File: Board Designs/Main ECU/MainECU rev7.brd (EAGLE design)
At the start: 120.6 x 78.9 mm, 202 parts, among them J1 JUMPER, J2 JUMPER, J3 JUMPER, J4 JUMPER, J5 JUMPER, J6 JUMPER, J7 JUMPER, J8 JUMPER, P1 SOLDER_PAD, P2 SOLDER_PAD, Q1 P-CHANNEL_MOSFET_DMP3099L-7, Q12 P-CHANNEL_MOSFET_DMP3099L-7, X1 CONNECTOR-37, X2 CONNECTOR-4AUTOSPORT, X3 CONNECTOR-4NANO-FIT-VERTICAL-4, X4 CONNECTOR-4NANO-FIT-VERTICAL-4

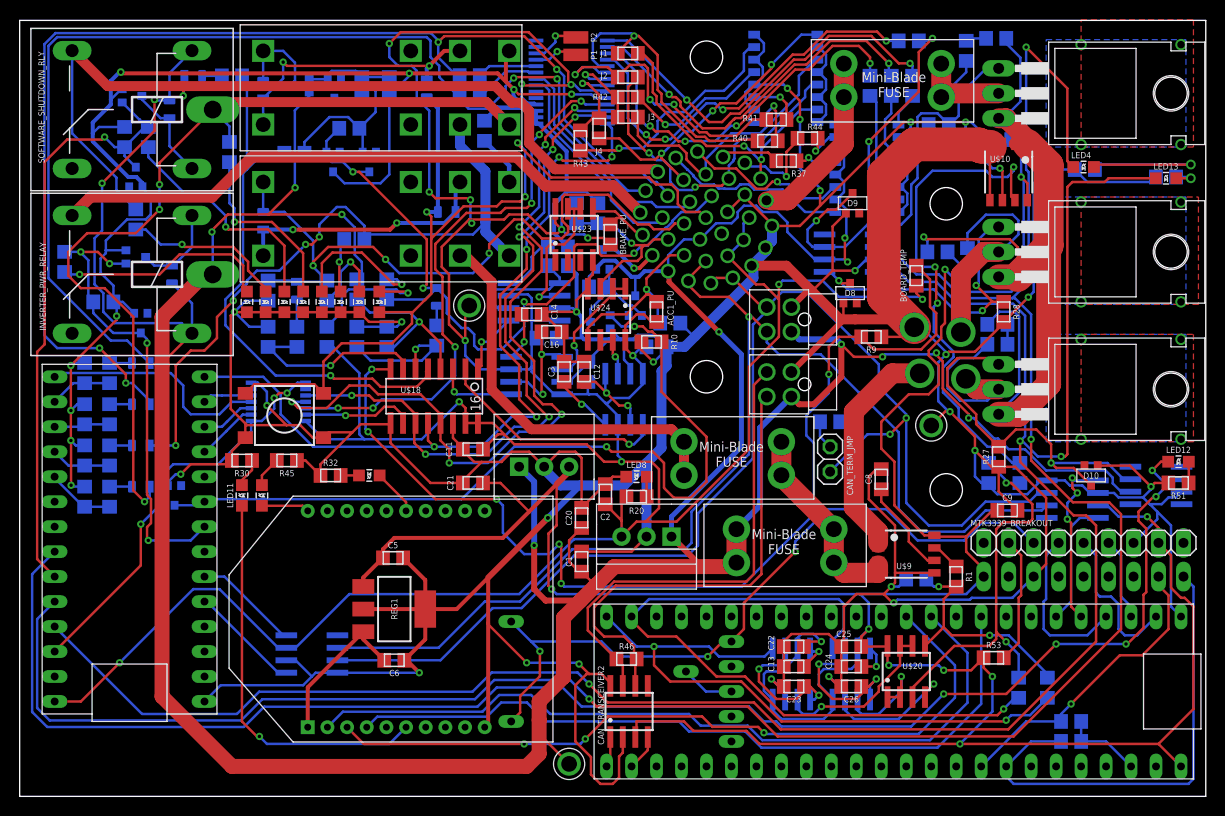
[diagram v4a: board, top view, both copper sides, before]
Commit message: Make silkscreen names larger
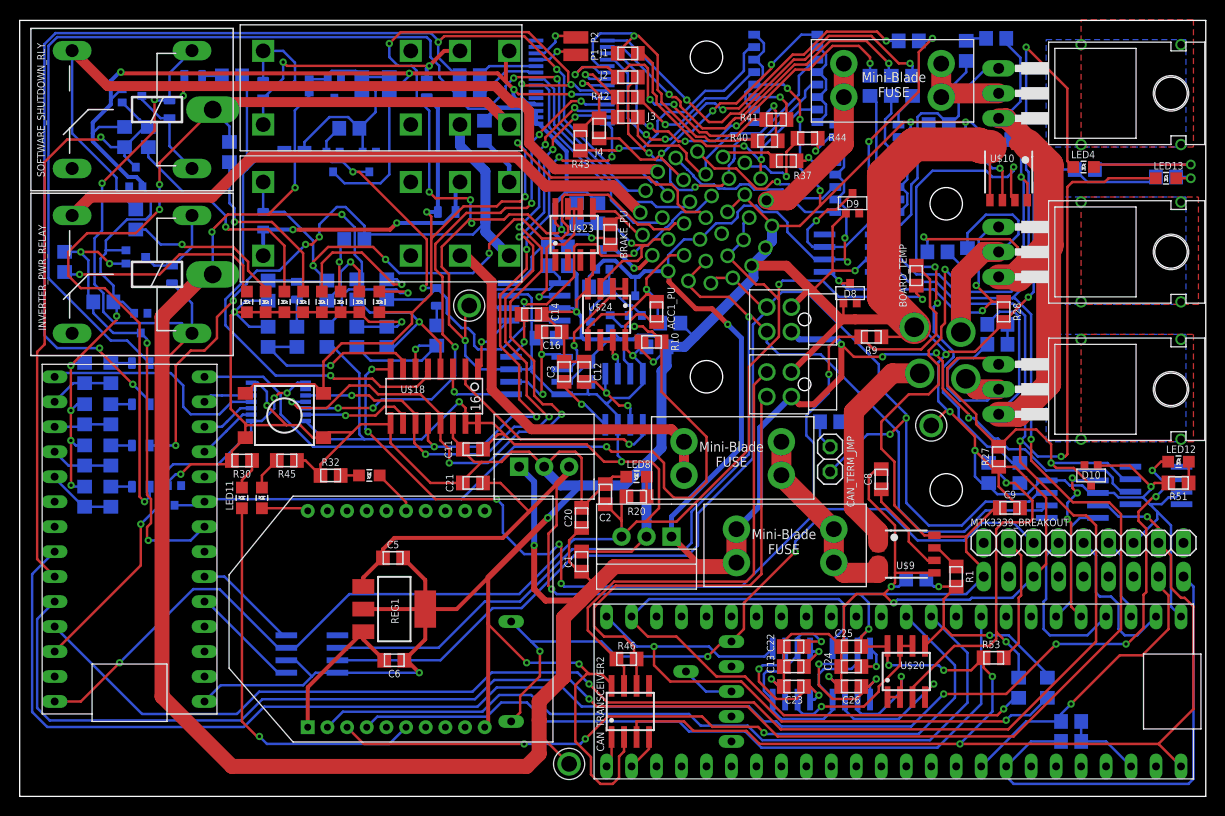
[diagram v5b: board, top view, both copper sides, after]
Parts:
- moved C9 0.36 mm to (100.7, 29.3)
- moved LED11 0.25 mm to (22.6, 30.4)
- moved LED14 0.25 mm to (24.6, 30.4)
- moved CAN_TRANSCEIVER2 0.13 mm to (62.1, 8.64)
- moved R11 0.13 mm to (9.27, 43.1)
- moved R57 0.13 mm to (9.27, 38.9)
- moved R59 0.13 mm to (9.27, 34.7)
- moved R61 0.13 mm to (9.27, 30.5)
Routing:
- net +12V: track 430.3 -> 431.2 mm
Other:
- board text added: "HyTech 2019 Main ECU rev7"
- board text removed: "HyTech 2019 Main ECU rev6"

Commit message: Merged SOT23 package update
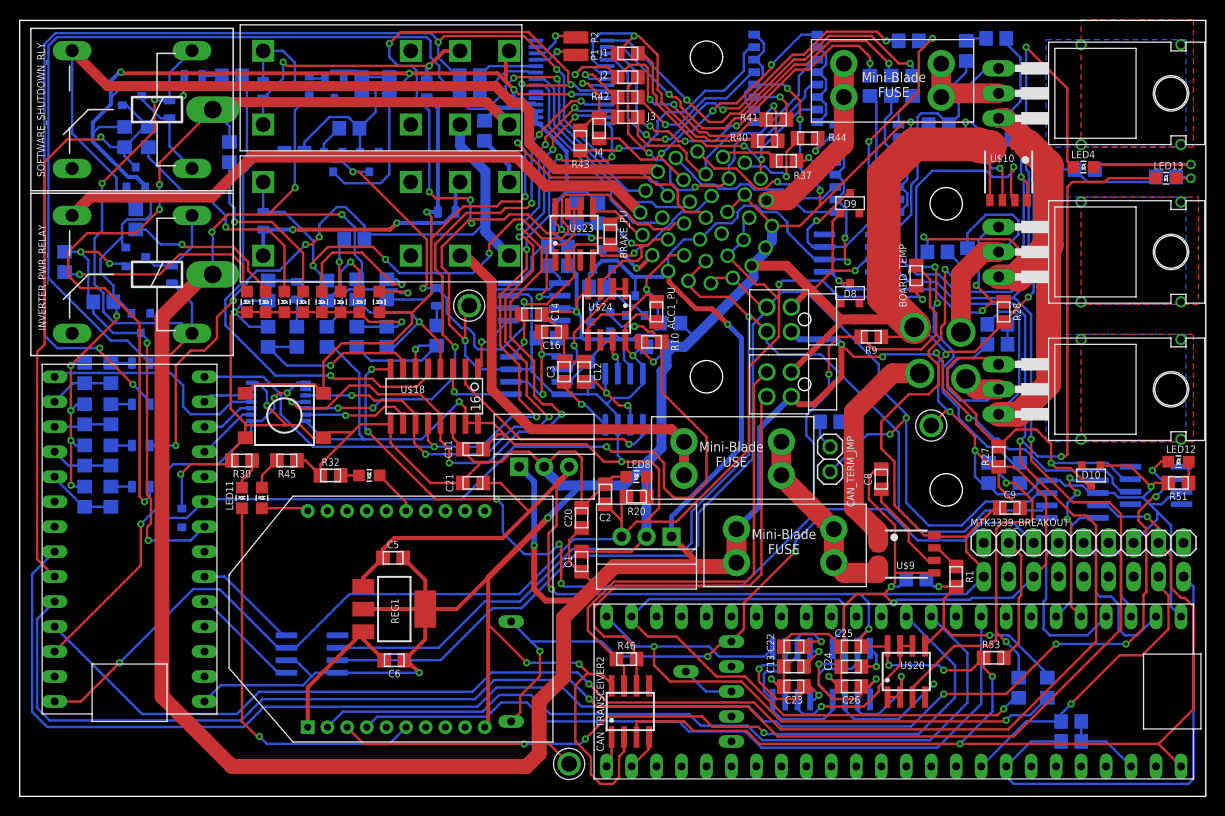
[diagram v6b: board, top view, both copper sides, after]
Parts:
- moved D12 2.30 mm to (15.5, 28.3), turned to 270 degrees
- moved D9 0.25 mm to (84.5, 60.3)
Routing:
- net BRAKE_LIGHT_CTRL: track 83.4 -> 85.5 mm
- net GND: track 918.5 -> 917.5 mm

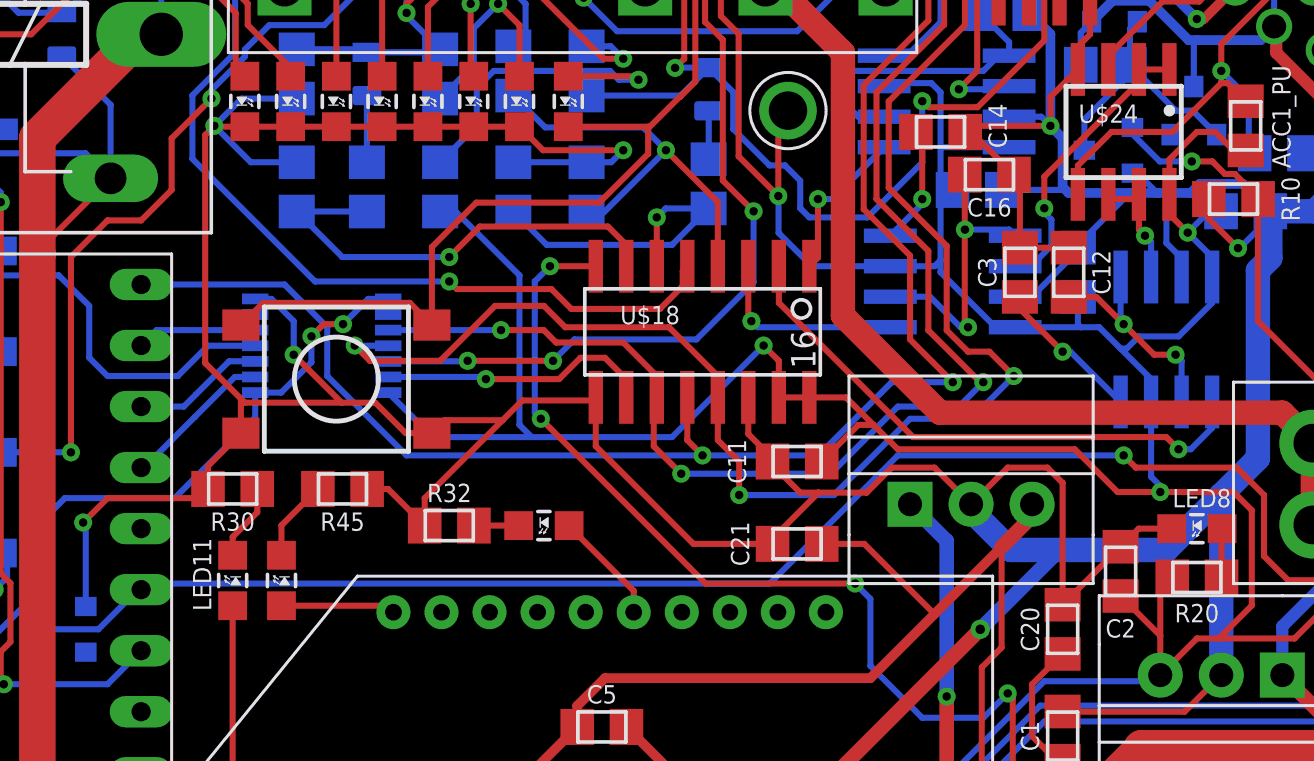
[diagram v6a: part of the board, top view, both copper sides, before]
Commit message: Added second 0.1 capacitor and began moving traces
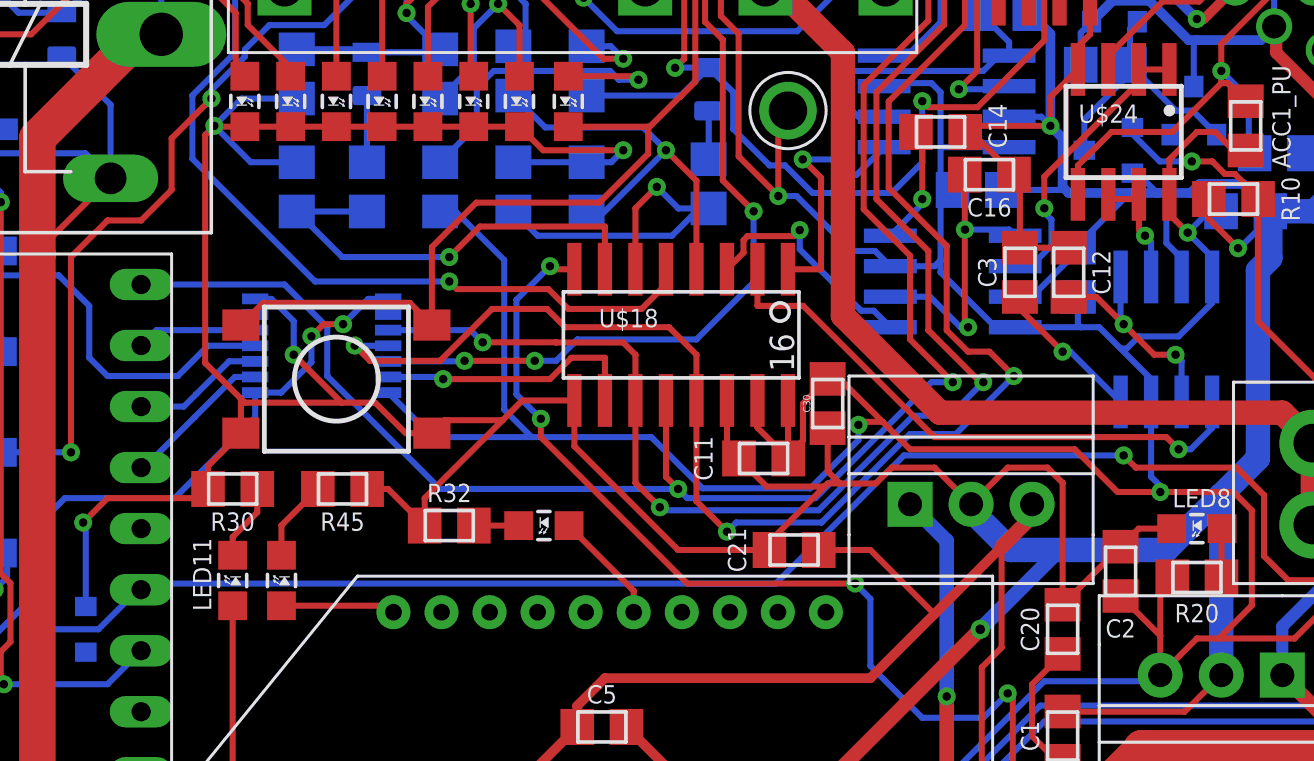
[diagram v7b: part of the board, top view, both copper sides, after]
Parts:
- added C30: 0.1uF, HyTechDevices:0805
- moved C11 1.40 mm to (44.7, 35.4)
- moved U$18 0.90 mm to (41.3, 40.5)
- moved C21 0.28 mm to (46.0, 31.6)
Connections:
- net +5V: now also C30.2
- net GND: now also C30.1
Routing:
- net +5V: track 357.4 -> 364.7 mm
- net READ_BRAKE: track 6.59 -> 10.4 mm
- net GND: track 917.5 -> 921.2 mm
- net MISO_TEENSY: track 81.6 -> 84.3 mm
- net MOSI_5V: track 70.9 -> 73.4 mm
- net SCK_5V: track 79.7 -> 82.1 mm
- net READ_ACCEL2: track 8.23 -> 9.92 mm
- net BMS_OK_READ: track 13.7 -> 15.3 mm
- net BMS_OK: track 74.4 -> 72.9 mm
- net SHUTDOWN_OUT_READ: track 55.3 -> 54.3 mm
- net READ_ACCEL1: track 23.5 -> 24.4 mm

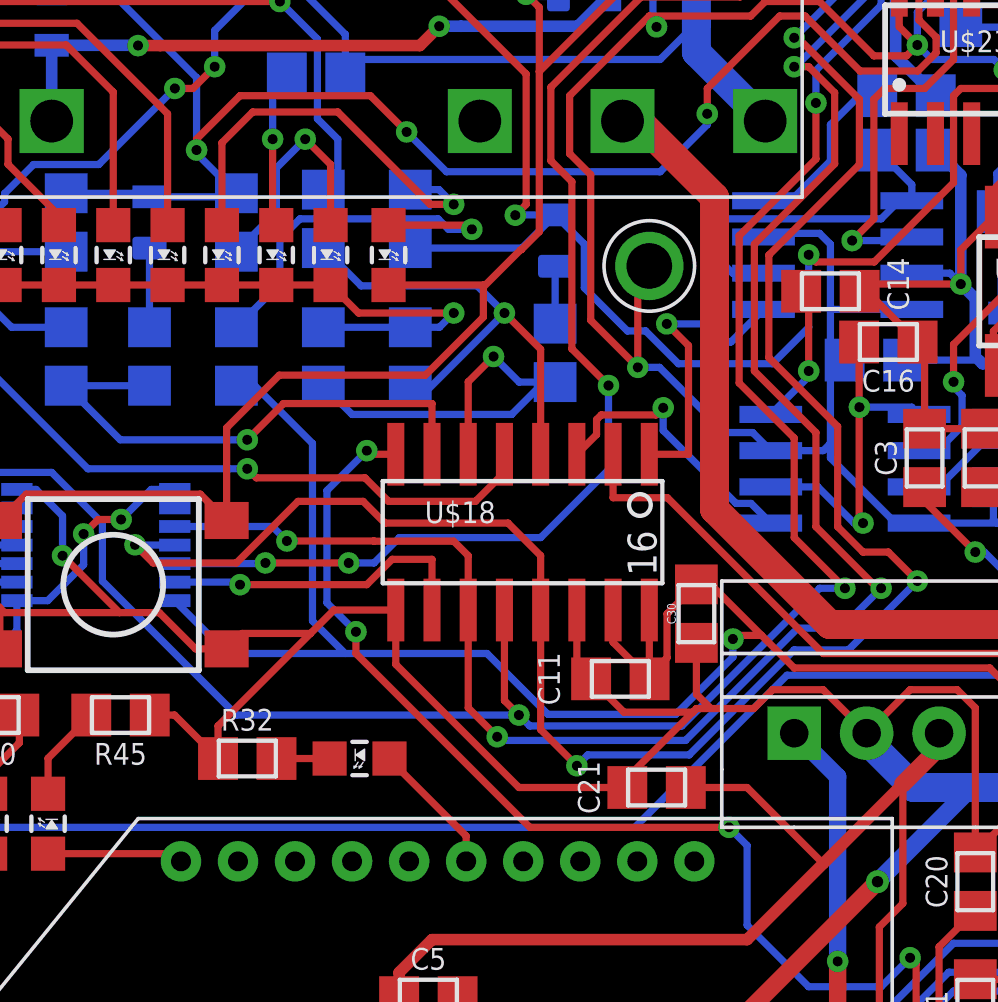
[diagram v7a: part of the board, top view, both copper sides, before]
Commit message: Finished routing to avoid ADC and bypass capacitors to help reduce noise
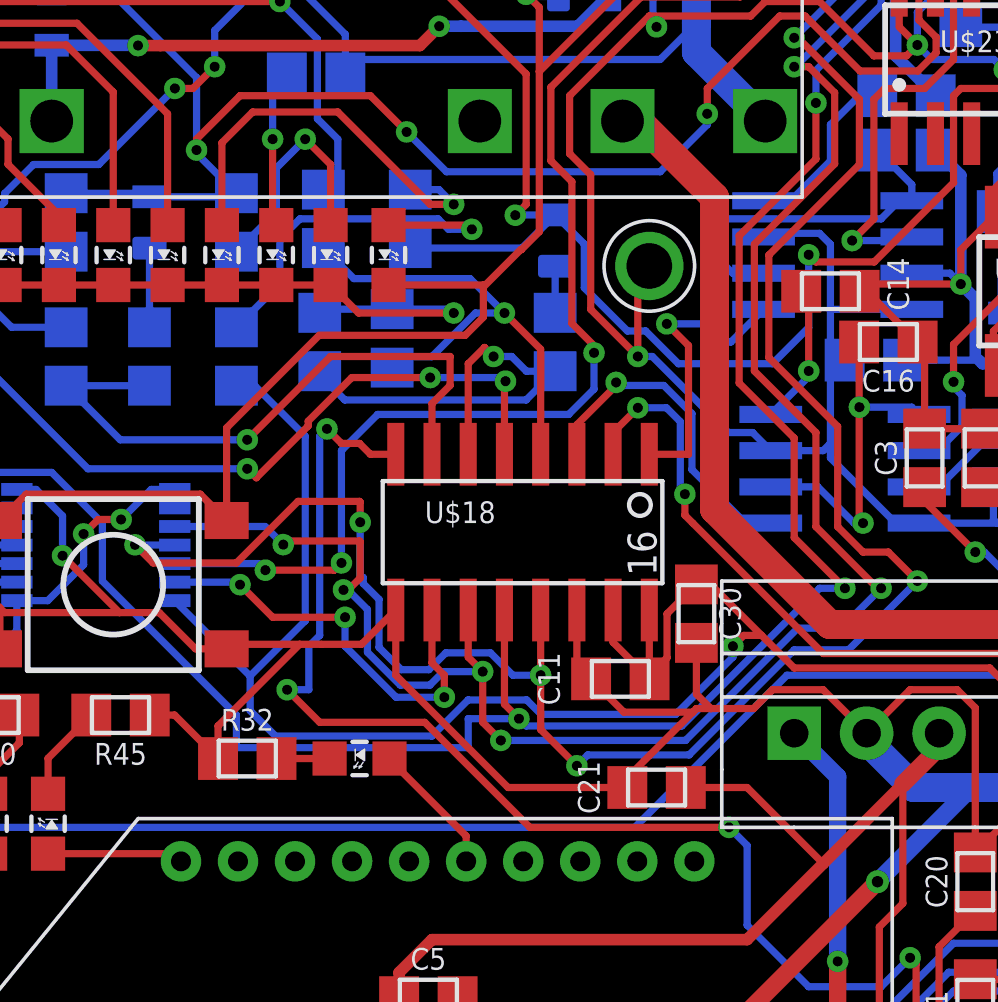
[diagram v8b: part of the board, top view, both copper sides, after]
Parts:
- moved R29 0.90 mm to (36.7, 47.4)
- moved R8 0.52 mm to (34.2, 47.2)
- moved R7 0.38 mm to (42.4, 47.2)
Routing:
- net TEMPSENSE: track 107.1 -> 112.8 mm
- net SCK_5V: track 82.1 -> 85.8 mm, vias 6 -> 8
- net CS1_5V: track 11.2 -> 15.0 mm, vias 1 -> 3
- net SHUTDOWN_OUT_READ: track 54.3 -> 58.0 mm, vias 1 -> 3
- net MOSI_5V: track 73.4 -> 77.0 mm, vias 6 -> 8
- net OKHS_READ: track 18.8 -> 22.1 mm
- net READ_ACCEL1: track 24.4 -> 27.1 mm, vias 1 -> 3
- net MISO_TEENSY: track 84.3 -> 86.5 mm
- net +5V: track 364.7 -> 366.7 mm
- net READ_ACCEL2: track 9.92 -> 11.7 mm
- net BMS_OK_READ: track 15.3 -> 16.0 mm
